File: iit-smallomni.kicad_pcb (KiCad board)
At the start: 2 copper layers, 100 x 100 mm, 83 parts, among them J1 Battery, J10 DC-Motor, J2 HC_SR04, J3 HC_SR04, J4 HC_SR04, J5 DC-Motor, J6 DC-Motor, J7 DC-Motor, J8 DC-Motor, J9 DC-Motor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

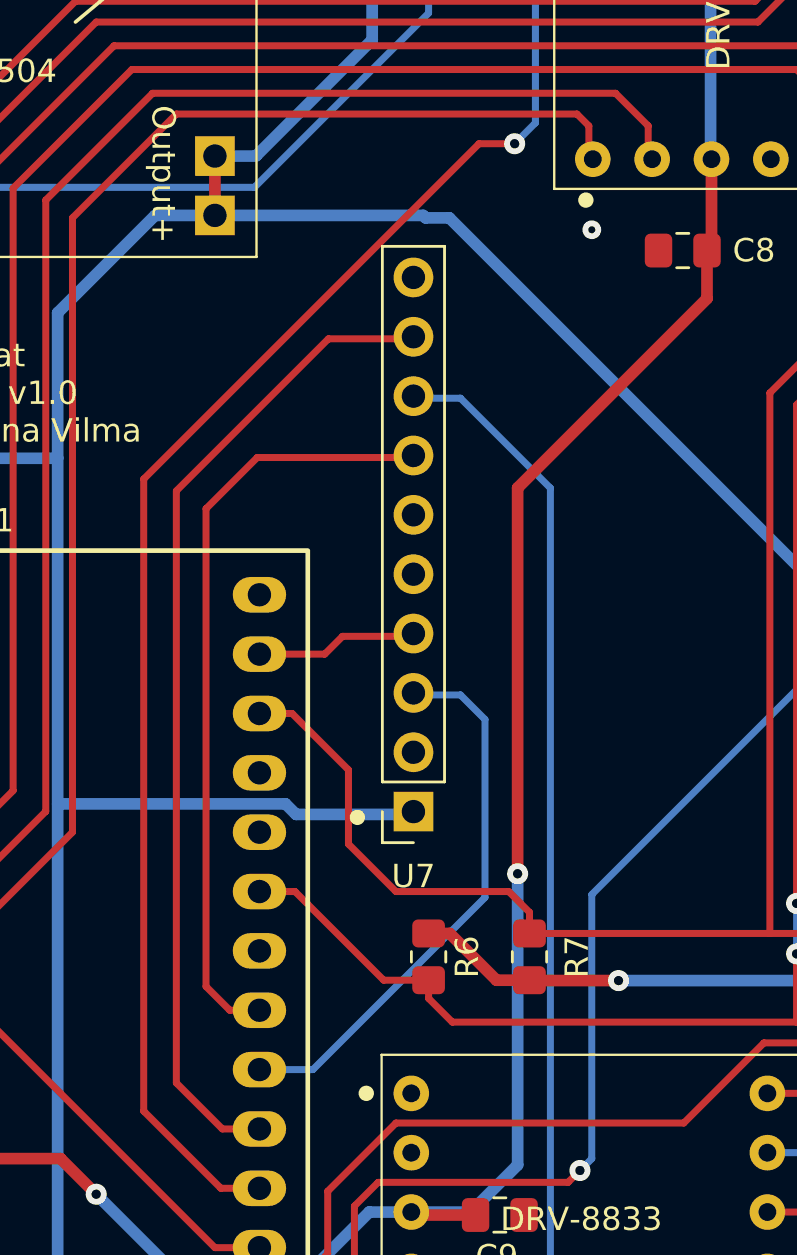
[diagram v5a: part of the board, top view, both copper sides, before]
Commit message: Fix MPU9250 orientation
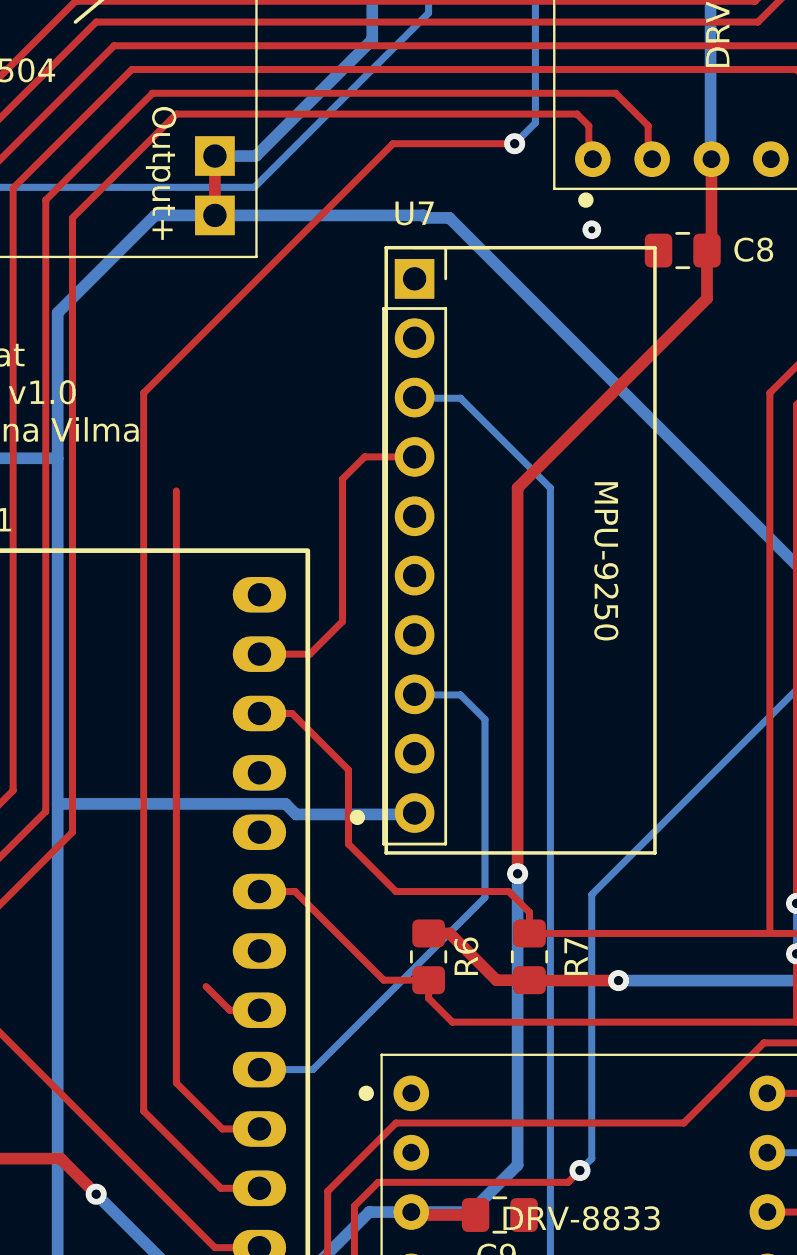
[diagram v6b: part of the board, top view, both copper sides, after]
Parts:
- moved U7 22.8 mm to (158.0, 65.6), turned to 0 degrees
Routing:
- net /MISO: track 33.1 -> 2.75 mm
- net /nCS: track 42.7 -> 29.7 mm
- net /MOSI: track 7.09 -> 13.7 mm
- net /UV_Echo_1: track 82.4 -> 84.5 mm
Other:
- board text added: "MPU-9250"
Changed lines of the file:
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@@
 	(footprint "Connector_PinSocket_2.54mm:PinSocket_1x10_P2.54mm_Vertical"
 		(layer "F.Cu")
-		(at 157.975 88.4 180)
+		(at 158.025 65.6)
 		(descr "Through hole straight socket strip, 1x10, 2.54mm pitch, single row (from Kicad 4.0.7), script generated")
 		(tags "Through hole socket strip THT 1x10 2.54mm single row")
 		(property "Reference" "U7"
-			(at 0 -2.77 180)
+			(at 0 -2.77 360)
 			(layer "F.SilkS")
 			(effects
@@
 		)
 		(property "Value" "MPU-9250_IMU"
-			(at 0 25.63 180)
+			(at 0 25.63 360)
 			(layer "F.Fab")
 			(effects
@@
 		)
 		(property "Footprint" "Connector_PinSocket_2.54mm:PinSocket_1x10_P2.54mm_Vertical"
-			(at 0 0 180)
+			(at 0 0 0)
 			(unlocked yes)
 			(layer "F.Fab")
@@
 		)
 		(property "Datasheet" ""
-			(at 0 0 180)
+			(at 0 0 0)
 			(unlocked yes)
 			(layer "F.Fab")
@@
 		)
 		(property "Description" ""
-			(at 0 0 180)
+			(at 0 0 0)
 			(unlocked yes)
 			(layer "F.Fab")
@@
 		(attr through_hole)
 		(fp_line
-			(start 1.33 1.27)
-			(end 1.33 24.19)
+			(start -1.33 1.27)
+			(end -1.33 24.19)
 			(stroke
 				(width 0.12)
@@
 		)
 		(fp_line
-			(start 1.33 -1.33)
-			(end 1.33 0)
+			(start -1.33 1.27)
+			(end 1.33 1.27)
 			(stroke
 				(width 0.12)
@@
 		)
 		(fp_line
-			(start 0 -1.33)
-			(end 1.33 -1.33)
+			(start -1.33 24.19)
+			(end 1.33 24.19)
 			(stroke
 				(width 0.12)
@@
 		)
 		(fp_line
-			(start -1.33 24.19)
-			(end 1.33 24.19)
+			(start 0 -1.33)
+			(end 1.33 -1.33)
 			(stroke
 				(width 0.12)
@@
 		)
 		(fp_line
-			(start -1.33 1.27)
-			(end 1.33 1.27)
+			(start 1.33 -1.33)
+			(end 1.33 0)
 			(stroke
 				(width 0.12)
@@
 		)
 		(fp_line
-			(start -1.33 1.27)
-			(end -1.33 24.19)
+			(start 1.33 1.27)
+			(end 1.33 24.19)
 			(stroke
 				(width 0.12)
@@
 		)
 		(fp_line
-			(start 1.75 24.6)
-			(end -1.8 24.6)
+			(start -1.8 -1.8)
+			(end 1.75 -1.8)
 			(stroke
 				(width 0.05)
@@
 		)
 		(fp_line
-			(start 1.75 -1.8)
-			(end 1.75 24.6)
+			(start -1.8 24.6)
+			(end -1.8 -1.8)
 			(stroke
 				(width 0.05)
@@
 		)
 		(fp_line
-			(start -1.8 24.6)
-			(end -1.8 -1.8)
+			(start 1.75 -1.8)
+			(end 1.75 24.6)
 			(stroke
 				(width 0.05)
@@
 		)
 		(fp_line
-			(start -1.8 -1.8)
-			(end 1.75 -1.8)
+			(start 1.75 24.6)
+			(end -1.8 24.6)
 			(stroke
 				(width 0.05)
@@
 		)
 		(fp_line
-			(start 1.27 24.13)
-			(end -1.27 24.13)
+			(start -1.27 -1.27)
+			(end 0.635 -1.27)
 			(stroke
 				(width 0.1)
@@
 		)
 		(fp_line
-			(start 1.27 -0.635)
-			(end 1.27 24.13)
+			(start -1.27 24.13)
+			(end -1.27 -1.27)
 			(stroke
 				(width 0.1)
@@
 		)
 		(fp_line
-			(start -1.27 24.13)
-			(end -1.27 -1.27)
+			(start 1.27 -0.635)
+			(end 1.27 24.13)
 			(stroke
 				(width 0.1)
@@
 		)
 		(fp_line
-			(start -1.27 -1.27)
-			(end 0.635 -1.27)
+			(start 1.27 24.13)
+			(end -1.27 24.13)
 			(stroke
 				(width 0.1)
@@
 		)
 		(fp_text user "${REFERENCE}"
-			(at 0 11.43 -90)
+			(at 0 11.43 90)
 			(layer "F.Fab")
 			(effects
@@
 		)
 		(pad "1" thru_hole rect
-			(at 0 0 180)
+			(at 0 0)
 			(size 1.7 1.7)
 			(drill 1)
@@
 		)
 		(pad "2" thru_hole oval
-			(at 0 2.54 180)
+			(at 0 2.54)
 			(size 1.7 1.7)
 			(drill 1)
@@
 		)
 		(pad "3" thru_hole oval
-			(at 0 5.08 180)
+			(at 0 5.08)
 			(size 1.7 1.7)
 			(drill 1)
@@
 		)
 		(pad "4" thru_hole oval
-			(at 0 7.62 180)
+			(at 0 7.62)
 			(size 1.7 1.7)
 			(drill 1)
@@
 		)
 		(pad "5" thru_hole oval
-			(at 0 10.16 180)
+			(at 0 10.16)
 			(size 1.7 1.7)
 			(drill 1)
@@
 		)
 		(pad "6" thru_hole oval
-			(at 0 12.7 180)
+			(at 0 12.7)
 			(size 1.7 1.7)
 			(drill 1)
@@
 		)
 		(pad "7" thru_hole oval
-			(at 0 15.24 180)
+			(at 0 15.24)
 			(size 1.7 1.7)
 			(drill 1)
@@
 		)
 		(pad "8" thru_hole oval
-			(at 0 17.78 180)
+			(at 0 17.78)
 			(size 1.7 1.7)
 			(drill 1)
@@
 		)
 		(pad "9" thru_hole oval
-			(at 0 20.32 180)
+			(at 0 20.32)
 			(size 1.7 1.7)
 			(drill 1)
@@
 		)
 		(pad "10" thru_hole oval
-			(at 0 22.86 180)
+			(at 0 22.86)
 			(size 1.7 1.7)
 			(drill 1)
@@
 		(layer "F.SilkS")
 	)
+	(gr_rect
+		(start 156.81 64.268786)
+		(end 168.31 90.168786)
+		(stroke
+			(width 0.15)
+			(type default)
+		)
+		(fill none)
+		(layer "F.SilkS")
+	)
 	(gr_line
 		(start 145.034 53.34)
@@
 		)
 	)
+	(gr_text "MPU-9250"
+		(at 165.608 74.168 -90)
+		(layer "F.SilkS")
+		(effects
+			(font
+				(size 1 1)
+				(thickness 0.15)
+			)
+			(justify left bottom)
+		)
+	)
 	(gr_text "Input+"
 		(at 133.731 64.008 90)
@@
 	)
 	(segment
-		(start 160.782 59.817)
-		(end 146.431 74.168)
+		(start 163.195 41.148)
+		(end 163.195 36.814)
 		(width 0.3)
 		(layer "F.Cu")
@@
 	)
 	(segment
-		(start 163.195 41.148)
+		(start 163.179 36.83)
 		(end 163.195 36.814)
 		(width 0.3)
@@
 	)
 	(segment
-		(start 163.179 36.83)
-		(end 163.195 36.814)
+		(start 157.099 59.817)
+		(end 146.431 70.485)
 		(width 0.3)
 		(layer "F.Cu")
@@
 	)
 	(segment
-		(start 146.431 101.219)
-		(end 149.733 104.521)
+		(start 146.431 70.485)
+		(end 146.431 101.219)
 		(width 0.3)
 		(layer "F.Cu")
@@
 	(segment
 		(start 162.306 59.817)
-		(end 160.782 59.817)
+		(end 157.099 59.817)
 		(width 0.3)
 		(layer "F.Cu")
@@
 	)
 	(segment
-		(start 146.431 74.168)
-		(end 146.431 101.219)
+		(start 146.431 101.219)
+		(end 149.733 104.521)
 		(width 0.3)
 		(layer "F.Cu")
@@
 	)
 	(segment
-		(start 154.94 80.899)
-		(end 158.118 80.899)
+		(start 154.94 80.264)
+		(end 154.94 74.168)
 		(width 0.3)
 		(layer "F.Cu")
@@
 	)
 	(segment
-		(start 154.178 81.661)
-		(end 154.94 80.899)
+		(start 155.888 73.22)
+		(end 158.025 73.22)
 		(width 0.3)
 		(layer "F.Cu")
@@
 	)
 	(segment
-		(start 151.384 81.661)
-		(end 154.178 81.661)
+		(start 154.94 74.168)
+		(end 155.888 73.22)
 		(width 0.3)
 		(layer "F.Cu")
@@
 	)
 	(segment
-		(start 158.118 80.899)
-		(end 158.15 80.867)
+		(start 153.543 81.661)
+		(end 154.94 80.264)
 		(width 0.3)
 		(layer "F.Cu")
@@
 	)
 	(segment
-		(start 149.098 75.438)
-		(end 151.289 73.247)
+		(start 151.384 81.661)
+		(end 153.543 81.661)
 		(width 0.3)
 		(layer "F.Cu")
-		(net 63)
+		(net 62)
 	)
 	(segment
-		(start 151.289 73.247)
-		(end 158.15 73.247)
+		(start 158.118 80.899)
+		(end 158.15 80.867)
 		(width 0.3)
 		(layer "F.Cu")
@@
 	)
 	(segment
-		(start 149.098 95.885)
-		(end 149.098 75.438)
-		(width 0.3)
-		(layer "F.Cu")
-		(net 63)
-	)
-	(segment
 		(start 150.114 96.901)
 		(end 149.098 95.885)
@@
 	)
 	(segment
-		(start 147.828 74.676)
-		(end 154.337 68.167)
-		(width 0.3)
-		(layer "F.Cu")
-		(net 64)
-	)
-	(segment
 		(start 149.7965 101.981)
 		(end 147.828 100.0125)
 		(width 0.3)
 		(layer "F.Cu")
-		(net 64)
-	)
-	(segment
-		(start 154.337 68.167)
-		(end 158.15 68.167)
-		(width 0.3)
-		(layer "F.Cu")

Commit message: Edge & basic layout
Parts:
- removed G***: LOGO, Onlab:IIT_logo_15x15mm
- added H1: MountingHole, MountingHole:MountingHole_3.2mm_M3, F.Cu at (229.7, 116.5)
- added H2: MountingHole, MountingHole:MountingHole_3.2mm_M3, F.Cu at (170.3, 116.5)
- added H3: MountingHole, MountingHole:MountingHole_3.2mm_M3, F.Cu at (153.9, 40.1)
- added H4: MountingHole, MountingHole:MountingHole_3.2mm_M3, F.Cu at (245.9, 39.1)
- added J11: Conn_02x05_Odd_Even, Connector_IDC:IDC-Header_2x05_P2.54mm_Vertical, F.Cu at (164.6, 83.8)
- added J12: LiPo guard, Connector_PinSocket_2.54mm:PinSocket_1x04_P2.54mm_Vertical, F.Cu at (175.8, 21.6)
- C1, C2, C3, C4, C5, C8, D11, R10, R11, R12: moved to B.Cu
- J1: footprint Connector_Molex:Molex_KK-254_AE-6410-02A_1x02_P2.54mm_Vertical -> Connector_Molex:Molex_KK-254_AE-6410-04A_1x04_P2.54mm_Vertical
- J10, J8, J9: footprint iit-smallomni:motor -> iit-smallomni:legacy-motor
- JP1: footprint Connector:FanPinHeader_1x03_P2.54mm_Vertical -> Connector_PinHeader_2.54mm:PinHeader_1x03_P2.54mm_Vertical
- moved R27 130.2 mm to (247.9, 57.4)
- moved J5 129.4 mm to (246.1, 81.5)
- moved J3 127.4 mm to (243.5, 49.3), turned to -150 degrees
- moved Q2 126.5 mm to (247.3, 51.9), turned to 0 degrees
- moved R28 123.5 mm to (237.8, 36.1), turned to 0 degrees
- moved J8 120.6 mm to (235.3, 84.4), turned to 0 degrees
- moved R29 117.6 mm to (233.2, 37.2), turned to 0 degrees
- moved R30 115.5 mm to (233.2, 40.1), turned to 0 degrees
- moved SW5 101.7 mm to (218.9, 21.9)
- moved SW6 101.7 mm to (226.5, 21.9)
- moved SW7 101.7 mm to (234.1, 21.9)
- moved C2 97.9 mm to (222.9, 24.9), turned to 90 degrees
- moved C5 95.5 mm to (216.9, 102.1), turned to 90 degrees
- moved C3 94.0 mm to (219.9, 24.9), turned to 90 degrees
- moved R4 91.8 mm to (184.2, 38.4), turned to 90 degrees
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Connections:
- J1 pad 2: GND -> /Batt_2
- R22 pad 2: Net-(U1-P14/GPIO14/ADC2_CH6) -> Net-(U1-P33/GPIO33/ADC1_CH5)
- U1 pad 10: /Mot1_DrvA -> /Mot3_EncA
- U1 pad 11: /Battery level -> Net-(JP1-C)
- U1 pad 12: Net-(U1-P14/GPIO14/ADC2_CH6) -> /JTAG_TMS
- U1 pad 13: /Mot3_EncB -> /JTAG_TDI
- U1 pad 15: /Mot3_EncA -> /JTAG_TCK
- U1 pad 23: Net-(JP1-C) -> /JTAG_TDO
- U1 pad 24: /Mot3_DrvB -> /Mot3_DrvA
- U1 pad 25: /Mot3_DrvA -> /Mot2_DrvB
- U1 pad 7: /Mot2_DrvB -> /Battery level
- U1 pad 8: /Mot2_DrvA -> Net-(U1-P33/GPIO33/ADC1_CH5)
- U1 pad 9: /Mot1_DrvB -> /Mot3_EncB
- U5 pad 1: /Mot1_DrvA -> /JTAG_TCK
- U5 pad 2: /Mot1_DrvB -> /JTAG_TDI
- U5 pad 5: /Mot2_DrvA -> /JTAG_TMS
- U6 pad 6: /Mot3_DrvB -> /JTAG_TDO
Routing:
- net +3.3V: track 627.3 -> 0.00 mm, vias 4 -> 0
- net +5V: track 263.2 -> 0.00 mm, vias 4 -> 0
- net /Mot3_EncA: track 139.9 -> 0.00 mm
- net VCC: track 138.9 -> 0.00 mm, vias 3 -> 0
- net /Interrupt: track 138.8 -> 0.00 mm, vias 5 -> 0
- net /Mot3_EncB: track 129.5 -> 0.00 mm
- net /Mot2_EncB: track 125.4 -> 0.00 mm, vias 1 -> 0
- net /Mot2_EncA: track 119.7 -> 0.00 mm
- net /I2C_SCL: track 101.7 -> 0.00 mm
- net /I2C_SDA: track 98.4 -> 0.00 mm, vias 2 -> 0
- net /UV_Trig_2: track 94.1 -> 0.00 mm, vias 2 -> 0
- net /DRV1_FAULT: track 89.0 -> 0.00 mm, vias 1 -> 0
- net /Mot1_EncB: track 85.5 -> 0.00 mm
- net /UV_Echo_1: track 84.5 -> 0.00 mm, vias 2 -> 0
- net /Mot2_DrvB: track 83.5 -> 0.00 mm
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- removed copper zone on B.Cu, net GND
- removed copper zone on F.Cu, net GND
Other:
- board size 100 x 100 mm -> 110.5 x 110.5 mm
- board text removed: "+3.3V"
- board text removed: "+5V"
- board text removed: "Echo1"
- board text removed: "Echo2"
- board text removed: "Echo3"
- board text removed: "Enc1_A"
- board text removed: "Enc1_B"
- board text removed: "Enc2_A"
- board text removed: "Enc2_B"
- board text removed: "Enc3_A"
- board text removed: "Enc3_B"
- board text removed: "GND"
- board text removed: "IIT Robotcsapat Robot alaplap v1.0 Técsi Zsuzsanna Vilma 2024"
- board text removed: "Input+"
- board text removed: "Input-"
- board text removed: "MPU-9250"
- board text removed: "Mot1_A"
- board text removed: "Mot1_B"
- board text removed: "Mot2_A"
- board text removed: "Mot2_B"
- board text removed: "Mot3_A"
- board text removed: "Mot3_B"
- board text removed: "Output+"
- board text removed: "Output-"
- board text removed: "Trig1"
- board text removed: "Trig2"
- board text removed: "Trig3"

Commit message: Routing refinement around esp and i2c
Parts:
- C1, C2, C3, C4, C5, C8, D11, R10, R11, R12: moved to F.Cu
- J1: moved to B.Cu
- SW1, SW2: footprint Connector:FanPinHeader_1x03_P2.54mm_Vertical -> Connector_PinSocket_2.54mm:PinSocket_1x03_P2.54mm_Vertical
- moved J11 32.8 mm to (169.2, 116.3), turned to 90 degrees
- moved H2 31.7 mm to (158.0, 87.4)
- moved R7 29.7 mm to (224.6, 81.8)
- moved R6 27.2 mm to (223.5, 85.3)
- moved U7 25.5 mm to (188.6, 75.2), turned to 90 degrees
- moved SW1 23.8 mm to (184.4, 22.3)
- moved R5 23.2 mm to (220.0, 95.0), turned to 90 degrees
- moved D6 21.8 mm to (222.5, 117.3)
- moved R17 21.8 mm to (222.5, 113.3)
- moved D10 21.3 mm to (236.7, 117.4)
- moved R21 21.3 mm to (236.8, 113.3)
- moved R27 19.4 mm to (245.9, 38.1), turned to 180 degrees
- moved J10 19.3 mm to (196.6, 31.0)
- moved SW2 18.9 mm to (171.7, 22.3)
- moved C4 18.6 mm to (233.7, 33.0)
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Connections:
- R10 pad 1: Net-(U4-P7) -> Net-(U4-P1)
- R11 pad 1: Net-(U4-P6) -> Net-(U4-P2)
- R12 pad 1: Net-(U4-P5) -> Net-(U4-P3)
- R22 pad 2: Net-(U1-P33/GPIO33/ADC1_CH5) -> Net-(U1-P27/GPIO27/ADC2_CH7)
- R8 pad 2: Net-(U5-FAULT) -> Net-(U5-SLEEP)
- R9 pad 2: Net-(U6-FAULT) -> Net-(U6-SLEEP)
- SW3 pad 1: Net-(U4-P7) -> Net-(U4-P1)
- SW3 pad 2: Net-(U4-P6) -> Net-(U4-P2)
- SW3 pad 3: Net-(U4-P5) -> Net-(U4-P3)
- U1 pad 10: /Mot3_EncA -> /UV_Echo_1
- U1 pad 11: Net-(JP1-C) -> Net-(U1-P27/GPIO27/ADC2_CH7)
- U1 pad 24: /Mot3_DrvA -> /UV_Echo_2
- U1 pad 25: /Mot2_DrvB -> /Mot1_DrvB
- U1 pad 26: /UV_Echo_3 -> /Mot1_EncB
- U1 pad 27: /UV_Echo_2 -> /Mot1_EncA
- U1 pad 28: /UV_Echo_1 -> /Mot3_DrvB
- U1 pad 3: /Mot1_EncA -> /Mot2_EncB
- U1 pad 4: /Mot1_EncB -> /Mot2_EncA
- U1 pad 5: /Mot2_EncA -> /UV_Echo_3
- U1 pad 6: /Mot2_EncB -> /Battery level
- U1 pad 7: /Battery level -> /Mot3_EncB
- U1 pad 8: Net-(U1-P33/GPIO33/ADC1_CH5) -> /Mot3_EncA
- U1 pad 9: /Mot3_EncB -> Net-(JP1-C)
- U4 pad 10: Net-(U4-P5) -> /Button_2
- U4 pad 11: Net-(U4-P6) -> /Button_1
- U4 pad 12: Net-(U4-P7) -> /DRV2_FAULT
- U4 pad 5: /DRV2_FAULT -> Net-(U4-P1)
- U4 pad 6: /Button_1 -> Net-(U4-P2)
- U4 pad 7: /Button_2 -> Net-(U4-P3)
- U5 pad 1: /JTAG_TCK -> /JTAG_TDO
- U5 pad 10: /Mot2_A -> unconnected-(U5-OUT3-Pad10)
- U5 pad 11: /Mot2_B -> unconnected-(U5-OUT4-Pad11)
- U5 pad 12: Net-(U5-FAULT) -> /DRV1_FAULT
- U5 pad 2: /JTAG_TDI -> /Mot1_DrvB
- U5 pad 5: /JTAG_TMS -> unconnected-(U5-IN3-Pad5)
- U5 pad 6: /Mot2_DrvB -> unconnected-(U5-IN4-Pad6)
- U5 pad 7: /DRV1_FAULT -> Net-(U5-SLEEP)
- U6 pad 1: unconnected-(U6-IN1-Pad1) -> /JTAG_TDI
- U6 pad 10: /Mot3_B -> /Mot3_A
- U6 pad 11: /Mot3_A -> /Mot3_B
- U6 pad 12: Net-(U6-FAULT) -> /DRV2_FAULT
- U6 pad 2: unconnected-(U6-IN2-Pad2) -> /JTAG_TMS
- U6 pad 5: /Mot3_DrvA -> /JTAG_TCK
- U6 pad 6: /JTAG_TDO -> /Mot3_DrvB
- U6 pad 7: /DRV2_FAULT -> Net-(U6-SLEEP)
- U6 pad 8: unconnected-(U6-OUT1-Pad8) -> /Mot2_B
- U6 pad 9: unconnected-(U6-OUT2-Pad9) -> /Mot2_A
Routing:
- net +3.3V: track 0.00 -> 280.9 mm, vias 0 -> 1
- net /Mot3_EncA: track 0.00 -> 128.6 mm
- net /Mot3_EncB: track 0.00 -> 124.7 mm
- net /I2C_SCL: track 0.00 -> 114.7 mm
- net /I2C_SDA: track 0.00 -> 105.4 mm
- net /UV_Echo_2: track 0.00 -> 74.8 mm, vias 0 -> 2
- net /Interrupt: track 0.00 -> 71.3 mm
- net /UV_Echo_3: track 0.00 -> 67.3 mm
- net /JTAG_TCK: track 0.00 -> 65.1 mm
- net /Mot1_EncA: track 0.00 -> 63.2 mm, vias 0 -> 2
- net /Mot1_EncB: track 0.00 -> 60.9 mm, vias 0 -> 2
- net /JTAG_TMS: track 0.00 -> 58.8 mm
- net +5V: track 0.00 -> 58.8 mm
- net /UV_Trig_2: track 0.00 -> 58.0 mm
- net /DRV2_FAULT: track 0.00 -> 56.5 mm
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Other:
- board size 110.5 x 110.5 mm -> 100 x 100 mm
